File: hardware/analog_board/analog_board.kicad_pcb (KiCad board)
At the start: 4 copper layers, 105 parts, among them J1 2x5 牛角座, U1 GW2A-LV18EQ144, U2 W25Q32JVSS, U3 AD9747BCPZ

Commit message: feat：重构滤波器预布局
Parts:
- added C100: 10uF, Capacitor_SMD:C_0603_1608Metric, F.Cu at (95.8, 158.8)
- added C101: 100nF, Capacitor_SMD:C_0603_1608Metric, F.Cu at (82.9, 144.1)
- added C102: 100nF, Capacitor_SMD:C_0603_1608Metric, F.Cu at (82.9, 146.6)
- added C103: 10uF, Capacitor_SMD:C_0603_1608Metric, F.Cu at (82.9, 149.1)
- added C104: 10uF, Capacitor_SMD:C_0603_1608Metric, F.Cu at (82.8, 140.9)
- added C105: 100nF, Capacitor_SMD:C_0603_1608Metric, F.Cu at (154.7, 160.2)
- added C106: 100nF, Capacitor_SMD:C_0603_1608Metric, F.Cu at (154.7, 162.7)
- added C107: 10uF, Capacitor_SMD:C_0603_1608Metric, F.Cu at (154.7, 165.2)
- added C108: 10uF, Capacitor_SMD:C_0603_1608Metric, F.Cu at (154.7, 167.7)
- added C109: 100nF, Capacitor_SMD:C_0603_1608Metric, F.Cu at (145.2, 48.3)
- added C110: 470nF, Capacitor_SMD:C_0603_1608Metric, F.Cu at (155.0, 94.0)
- added C111: 100nF, Capacitor_SMD:C_0603_1608Metric, F.Cu at (155.0, 96.5)
- added C112: 4.7uF, Capacitor_SMD:C_0603_1608Metric, F.Cu at (155.0, 99.0)
- added C113: 470nF, Capacitor_SMD:C_0603_1608Metric, F.Cu at (155.0, 101.5)
- added C114: 100nF, Capacitor_SMD:C_0603_1608Metric, F.Cu at (159.0, 91.5)
- added C115: 4.7uF, Capacitor_SMD:C_0603_1608Metric, F.Cu at (159.0, 94.0)
- added C116: 470nF, Capacitor_SMD:C_0603_1608Metric, F.Cu at (159.0, 96.5)
- added C117: 100nF, Capacitor_SMD:C_0603_1608Metric, F.Cu at (159.0, 99.0)
- added C118: 4.7uF, Capacitor_SMD:C_0603_1608Metric, F.Cu at (159.0, 101.5)
- added C119: 470nF, Capacitor_SMD:C_0603_1608Metric, F.Cu at (163.0, 91.5)
- added C120: 100nF, Capacitor_SMD:C_0603_1608Metric, F.Cu at (163.0, 94.0)
- added C121: 100nF, Capacitor_SMD:C_0603_1608Metric, F.Cu at (214.5, 104.8)
- added C122: 100nF, Capacitor_SMD:C_0603_1608Metric, F.Cu at (214.5, 107.3)
- added C123: 330pF, Capacitor_SMD:C_0603_1608Metric, F.Cu at (214.5, 109.8)
- added C124: 33nF, Capacitor_SMD:C_0603_1608Metric, F.Cu at (214.5, 112.4)
- added C125: 1uF, Capacitor_SMD:C_0603_1608Metric, F.Cu at (214.5, 114.9)
- added C126: 1uF, Capacitor_SMD:C_0603_1608Metric, F.Cu at (214.5, 117.4)
- added C128: 100uF, Capacitor_SMD:C_Elec_6.3x7.7, F.Cu at (217.4, 66.9)
- added C129: 1uF, Capacitor_SMD:C_0603_1608Metric, F.Cu at (214.5, 119.9)
- added C130: 1uF, Capacitor_SMD:C_0603_1608Metric, F.Cu at (214.5, 122.4)
- added C131: 100nF, Capacitor_SMD:C_0603_1608Metric, F.Cu at (214.5, 124.9)
- added C133: 1uF, Capacitor_SMD:C_0603_1608Metric, F.Cu at (214.5, 127.4)
- added C134: 1uF, Capacitor_SMD:C_0603_1608Metric, F.Cu at (218.5, 104.8)
- added C135: 100nF, Capacitor_SMD:C_0603_1608Metric, F.Cu at (218.5, 107.3)
- added C136: 100nF, Capacitor_SMD:C_0603_1608Metric, F.Cu at (218.5, 109.8)
- added C137: 1.2nF, Capacitor_SMD:C_0603_1608Metric, F.Cu at (218.5, 112.4)
- added C138: 2.2uF, Capacitor_SMD:C_0603_1608Metric, F.Cu at (218.5, 114.9)
- added C139: 100uF, Capacitor_SMD:C_Elec_6.3x7.7, F.Cu at (217.4, 75.0)
- added C140: 22uF, Capacitor_SMD:C_1206_3216Metric, F.Cu at (235.3, 105.2)
- added C141: 22uF, Capacitor_SMD:C_1206_3216Metric, F.Cu at (235.3, 108.6)
- added C142: 100nF, Capacitor_SMD:C_0603_1608Metric, F.Cu at (218.5, 117.4)
- added C143: 1uF, Capacitor_SMD:C_0603_1608Metric, F.Cu at (218.5, 119.9)
- added C145: 1uF, Capacitor_SMD:C_0603_1608Metric, F.Cu at (228.3, 36.6)
- added C146: 1uF, Capacitor_SMD:C_0603_1608Metric, F.Cu at (228.3, 39.1)
- added C147: 100nF, Capacitor_SMD:C_0603_1608Metric, F.Cu at (228.3, 41.6)
- added C148: 33nF, Capacitor_SMD:C_0603_1608Metric, F.Cu at (232.3, 19.0)
- added C149: 100nF, Capacitor_SMD:C_0603_1608Metric, F.Cu at (232.3, 21.5)
- added C150: 100uF, Capacitor_SMD:C_Elec_6.3x7.7, F.Cu at (217.4, 83.2)
- added C151: 100uF, Capacitor_SMD:C_Elec_6.3x7.7, F.Cu at (217.4, 91.3)
- added C152: 22uF, Capacitor_SMD:CP_Elec_5x5.4, F.Cu at (246.8, 35.3)
- added C153: 100nF, Capacitor_SMD:C_0603_1608Metric, F.Cu at (240.6, 25.9)
- added C154: 22uF, Capacitor_SMD:C_1206_3216Metric, F.Cu at (245.2, 26.1)
- added C155: 22uF, Capacitor_SMD:C_1206_3216Metric, F.Cu at (245.2, 29.5)
- added C156: 100uF, Capacitor_SMD:C_Elec_6.3x7.7, F.Cu at (217.4, 99.5)
- added C157: 100uF, Capacitor_SMD:C_Elec_6.3x7.7, F.Cu at (227.4, 66.9)
- added C158: 100nF, Capacitor_SMD:C_0603_1608Metric, F.Cu at (222.5, 112.4)
- added C159: 100nF, Capacitor_SMD:C_0603_1608Metric, F.Cu at (222.5, 114.9)
- added C160: 100uF, Capacitor_SMD:C_Elec_6.3x7.7, F.Cu at (227.4, 75.0)
- added C161: 100uF, Capacitor_SMD:C_Elec_6.3x7.7, F.Cu at (227.4, 83.2)
- added C162: 100nF, Capacitor_SMD:C_0603_1608Metric, F.Cu at (222.5, 117.4)
- added C163: 100nF, Capacitor_SMD:C_0603_1608Metric, F.Cu at (222.5, 119.9)
- added C164: 100uF, Capacitor_SMD:C_Elec_6.3x7.7, F.Cu at (227.4, 91.3)
- added C165: 100uF, Capacitor_SMD:C_Elec_6.3x7.7, F.Cu at (227.4, 99.5)
- added C166: 1uF, Capacitor_SMD:C_0603_1608Metric, F.Cu at (222.5, 122.4)
- added C167: 100uF, Capacitor_SMD:C_Elec_6.3x7.7, F.Cu at (237.3, 66.9)
- added C168: 100uF, Capacitor_SMD:C_Elec_6.3x7.7, F.Cu at (237.3, 75.0)
- added C169: 100nF, Capacitor_SMD:C_0603_1608Metric, F.Cu at (222.5, 124.9)
- added C170: 100uF, Capacitor_SMD:C_Elec_6.3x7.7, F.Cu at (237.3, 83.2)
- added C171: 100nF, Capacitor_SMD:C_0603_1608Metric, F.Cu at (222.5, 127.4)
- added C172: 100uF, Capacitor_SMD:C_Elec_6.3x7.7, F.Cu at (237.3, 91.3)
- added C173: 100nF, Capacitor_SMD:C_0603_1608Metric, F.Cu at (226.5, 104.8)
- added C174: 100nF, Capacitor_SMD:C_0603_1608Metric, F.Cu at (226.5, 107.3)
- added C175: 10uF, Capacitor_SMD:C_0603_1608Metric, F.Cu at (226.5, 109.8)
- added C176: 10uF, Capacitor_SMD:C_0603_1608Metric, F.Cu at (226.5, 112.4)
- added C177: 100nF, Capacitor_SMD:C_0603_1608Metric, F.Cu at (226.5, 114.9)
- added C178: 22uF, Capacitor_SMD:CP_Elec_5x5.4, F.Cu at (263.7, 104.9)
- added C179: 22uF, Capacitor_SMD:CP_Elec_5x5.4, F.Cu at (195.7, 91.9)
- added C61: 56pF, Capacitor_SMD:C_0603_1608Metric, F.Cu at (119.5, 100.4)
- added C62: 100pF, Capacitor_SMD:C_0603_1608Metric, F.Cu at (119.5, 102.5)
- added C63: 100pF, Capacitor_SMD:C_0603_1608Metric, F.Cu at (119.5, 106.1)
- added C64: 62pF, Capacitor_SMD:C_0603_1608Metric, F.Cu at (119.5, 109.7)
- added C65: 56pF, Capacitor_SMD:C_0603_1608Metric, F.Cu at (116.5, 100.4)
- added C66: 100pF, Capacitor_SMD:C_0603_1608Metric, F.Cu at (116.5, 102.5)
- added C67: 100pF, Capacitor_SMD:C_0603_1608Metric, F.Cu at (116.5, 106.1)
- added C68: 62pF, Capacitor_SMD:C_0603_1608Metric, F.Cu at (116.5, 109.7)
- added C69: 6.8p, Capacitor_SMD:C_0603_1608Metric, F.Cu at (123.5, 101.5)
- added C70: 9.1p, Capacitor_SMD:C_0603_1608Metric, F.Cu at (123.8, 104.9)
- added C71: 2.0p, Capacitor_SMD:C_0603_1608Metric, F.Cu at (123.7, 108.5)
- added C72: 6.8p, Capacitor_SMD:C_0603_1608Metric, F.Cu at (112.5, 101.4)
- added C73: 9.1p, Capacitor_SMD:C_0603_1608Metric, F.Cu at (112.3, 105.1)
- added C74: 2.0p, Capacitor_SMD:C_0603_1608Metric, F.Cu at (112.5, 108.5)
- added C75: 56pF, Capacitor_SMD:C_0603_1608Metric, F.Cu at (96.6, 100.3)
- added C76: 56pF, Capacitor_SMD:C_0603_1608Metric, F.Cu at (99.6, 100.3)
- added C77: 6.8p, Capacitor_SMD:C_0603_1608Metric, F.Cu at (92.6, 101.3)
- added C78: 6.8p, Capacitor_SMD:C_0603_1608Metric, F.Cu at (103.7, 101.4)
- added C79: 100pF, Capacitor_SMD:C_0603_1608Metric, F.Cu at (96.6, 103.9)
- added C80: 100pF, Capacitor_SMD:C_0603_1608Metric, F.Cu at (99.6, 103.9)
- added C81: 9.1p, Capacitor_SMD:C_0603_1608Metric, F.Cu at (92.5, 104.9)
- added C82: 9.1p, Capacitor_SMD:C_0603_1608Metric, F.Cu at (103.7, 104.9)
- added C83: 100pF, Capacitor_SMD:C_0603_1608Metric, F.Cu at (96.6, 107.4)
- added C84: 100pF, Capacitor_SMD:C_0603_1608Metric, F.Cu at (99.6, 107.4)
- added C85: 2.0p, Capacitor_SMD:C_0603_1608Metric, F.Cu at (92.4, 108.4)
- added C86: 2.0p, Capacitor_SMD:C_0603_1608Metric, F.Cu at (103.9, 108.6)
- added C87: 62pF, Capacitor_SMD:C_0603_1608Metric, F.Cu at (96.6, 109.5)
- added C88: 62pF, Capacitor_SMD:C_0603_1608Metric, F.Cu at (99.6, 109.5)
- added C89: 100nF, Capacitor_SMD:C_0603_1608Metric, F.Cu at (145.2, 50.8)
- added C90: 100n, Capacitor_SMD:C_0603_1608Metric, F.Cu at (146.1, 144.5)
- added C91: 100nF, Capacitor_SMD:C_0603_1608Metric, F.Cu at (146.1, 147.0)
- added C92: 100nF, Capacitor_SMD:C_0603_1608Metric, F.Cu at (146.1, 149.5)
- added C93: 100nF, Capacitor_SMD:C_0603_1608Metric, F.Cu at (146.1, 152.0)
- added C94: 100nF, Capacitor_SMD:C_0603_1608Metric, F.Cu at (150.1, 142.0)
- added C95: 100n, Capacitor_SMD:C_0603_1608Metric, F.Cu at (145.5, 159.0)
- added C96: 10uF, Capacitor_SMD:C_0603_1608Metric, F.Cu at (95.8, 151.3)
- added C97: 4.7uF, Capacitor_SMD:C_0603_1608Metric, F.Cu at (155.0, 91.5)
- added C98: 100nF, Capacitor_SMD:C_0603_1608Metric, F.Cu at (95.8, 153.8)
- added C99: 100nF, Capacitor_SMD:C_0603_1608Metric, F.Cu at (95.8, 156.3)
- added D2: SS34, Diode_SMD:D_SMA, F.Cu at (179.6, 85.4)
- added D3: SS34, Diode_SMD:D_SMA, F.Cu at (179.6, 89.9)
- added FB10: 600R@100MHz, Inductor_SMD:L_0603_1608Metric, F.Cu at (158.7, 165.2)
- added FB11: 600R@100MHz, Inductor_SMD:L_0603_1608Metric, F.Cu at (163.0, 99.0)
- added FB12: 600R@100MHz, Inductor_SMD:L_0603_1608Metric, F.Cu at (163.0, 101.5)
- added FB13: 600R@100MHz, Inductor_SMD:L_0603_1608Metric, F.Cu at (167.0, 91.5)
- added FB14: 600R@100MHz, Inductor_SMD:L_0603_1608Metric, F.Cu at (167.0, 94.0)
- added FB15: 600R@100MHz, Inductor_SMD:L_0603_1608Metric, F.Cu at (167.0, 96.5)
- added FB16: 600R@100MHz, Inductor_SMD:L_0603_1608Metric, F.Cu at (167.0, 99.0)
- added FB17: 600R@100MHz, Inductor_SMD:L_0603_1608Metric, F.Cu at (167.0, 101.5)
- added FB4: 600R@100MHz, Inductor_SMD:L_0603_1608Metric, F.Cu at (163.0, 96.5)
- added FB5: 600R@100MHz, Inductor_SMD:L_0603_1608Metric, F.Cu at (100.6, 156.8)
- added FB6: 600R@100MHz, Inductor_SMD:L_0603_1608Metric, F.Cu at (100.6, 159.3)
- added FB7: 600R@100MHz, Inductor_SMD:L_0603_1608Metric, F.Cu at (86.8, 140.9)
- added FB8: 600R@100MHz, Inductor_SMD:L_0603_1608Metric, F.Cu at (86.8, 143.4)
- added FB9: 600R@100MHz, Inductor_SMD:L_0603_1608Metric, F.Cu at (158.7, 162.7)
- added HS1: Heatsink_Pad, Heatsink:TO-220_Heatsink, F.Cu at (247.7, 75.1)
- added HS2: Heatsink_Pad, Heatsink:TO-220_Heatsink, F.Cu at (247.7, 88.1)
- added HS3: Heatsink_Pad, Heatsink:TO-220_Heatsink, F.Cu at (247.7, 101.1)
- added HS4: Heatsink_Pad, Heatsink:TO-220_Heatsink, F.Cu at (247.7, 114.1)
- added J2: Conn_02x08_Counter_Clockwise, Connector_IDC:IDC-Header_2x08_P2.54mm_Latch_Vertical, F.Cu at (280.4, 74.8)
- added J3: Conn_01x04_Pin, Connector_PinHeader_2.54mm:PinHeader_1x04_P2.54mm_Vertical, F.Cu at (277.5, 108.9)
- added J4: Conn_01x08, Connector_JST:JST_VH_B8P-VH_1x08_P3.96mm_Vertical, F.Cu at (290.5, 67.5)
- added L1: 160n, Inductor_SMD:L_0805_2012Metric, F.Cu at (121.9, 101.5)
- added L10: 180n, Inductor_SMD:L_0805_2012Metric, F.Cu at (102.0, 104.9)
- added L11: 180n, Inductor_SMD:L_0805_2012Metric, F.Cu at (94.2, 108.4)
- added L12: 180n, Inductor_SMD:L_0805_2012Metric, F.Cu at (102.0, 108.5)
- added L13: 33uH, Inductor_SMD:L_Changjiang_FXL1040, F.Cu at (249.9, 120.6)
- added L14: 150uH, Inductor_SMD:L_12x12mm_H6mm, F.Cu at (265.8, 93.7)
- added L15: 2.2uH, Inductor_SMD:L_Changjiang_FXL0420, F.Cu at (271.6, 34.2)
- added L2: 180n, Inductor_SMD:L_0805_2012Metric, F.Cu at (121.9, 105.0)
- added L3: 180n, Inductor_SMD:L_0805_2012Metric, F.Cu at (121.9, 108.6)
- added L4: 160n, Inductor_SMD:L_0805_2012Metric, F.Cu at (114.1, 101.5)
- added L5: 180n, Inductor_SMD:L_0805_2012Metric, F.Cu at (114.1, 105.0)
- added L6: 180n, Inductor_SMD:L_0805_2012Metric, F.Cu at (114.1, 108.6)
- added L7: 160n, Inductor_SMD:L_0805_2012Metric, F.Cu at (94.2, 101.3)
- added L8: 160n, Inductor_SMD:L_0805_2012Metric, F.Cu at (102.0, 101.4)
- added L9: 180n, Inductor_SMD:L_0805_2012Metric, F.Cu at (94.2, 104.9)
- added Q1: MMBT3906, Package_TO_SOT_SMD:SOT-23, F.Cu at (154.2, 144.0)
- added Q2: MMBT3906, Package_TO_SOT_SMD:SOT-23, F.Cu at (154.2, 149.6)
- added R29: 53.6R, Resistor_SMD:R_0603_1608Metric, F.Cu at (96.0, 161.8)
- added R30: 226R, Resistor_SMD:R_0603_1608Metric, F.Cu at (93.5, 161.8)
- added R31: 73.2R, Resistor_SMD:R_0603_1608Metric, F.Cu at (97.0, 165.8)
- added R32: 73.2R, Resistor_SMD:R_0603_1608Metric, F.Cu at (94.5, 165.8)
- added R33: 442R, Resistor_SMD:R_0603_1608Metric, F.Cu at (92.0, 165.8)
- added R34: 442R, Resistor_SMD:R_0603_1608Metric, F.Cu at (89.5, 165.8)
- added R35: 0R, Resistor_SMD:R_0603_1608Metric, B.Cu at (117.3, 96.6)
- added R36: 10kR, Resistor_SMD:R_0603_1608Metric, F.Cu at (119.5, 111.2)
- added R37: 10kR, Resistor_SMD:R_0603_1608Metric, F.Cu at (116.5, 111.2)
- added R38: 0R, Resistor_SMD:R_0603_1608Metric, B.Cu at (98.8, 96.5)
- added R39: 10kR, Resistor_SMD:R_0603_1608Metric, F.Cu at (96.6, 111.0)
- added R40: 10kR, Resistor_SMD:R_0603_1608Metric, F.Cu at (99.6, 111.0)
- added R41: 53.6R, Resistor_SMD:R_0603_1608Metric, F.Cu at (71.8, 146.8)
- added R42: 226R, Resistor_SMD:R_0603_1608Metric, F.Cu at (77.2, 147.5)
- added R43: 73.2R, Resistor_SMD:R_0603_1608Metric, F.Cu at (74.1, 147.6)
- added R44: 73.2R, Resistor_SMD:R_0603_1608Metric, F.Cu at (75.7, 147.6)
- added R45: 442R, Resistor_SMD:R_0603_1608Metric, F.Cu at (71.8, 148.3)
- added R46: 442R, Resistor_SMD:R_0603_1608Metric, F.Cu at (78.5, 152.8)
- added R47: 100R, Resistor_SMD:R_0603_1608Metric, F.Cu at (145.2, 45.8)
- added R48: 100R, Resistor_SMD:R_0603_1608Metric, F.Cu at (145.2, 43.3)
- added R49: 68R, Resistor_SMD:R_0603_1608Metric, F.Cu at (150.1, 149.5)
- added R50: 100R, Resistor_SMD:R_0603_1608Metric, F.Cu at (150.1, 152.0)
- added R51: 68R, Resistor_SMD:R_0603_1608Metric, F.Cu at (145.5, 161.5)
- added R52: 100R, Resistor_SMD:R_0603_1608Metric, F.Cu at (145.5, 164.0)
- added R53: 10kR, Resistor_SMD:R_0402_1005Metric, F.Cu at (141.7, 51.1)
- added R54: 4.7kR, Resistor_SMD:R_0402_1005Metric, F.Cu at (141.7, 49.1)
- added R55: 4.7kR, Resistor_SMD:R_0402_1005Metric, F.Cu at (141.7, 47.1)
- added R56: 4.7kR, Resistor_SMD:R_0402_1005Metric, F.Cu at (141.6, 44.1)
- added R57: 4.7kR, Resistor_SMD:R_0402_1005Metric, F.Cu at (141.6, 46.1)
- added R58: 22R, Resistor_SMD:R_0402_1005Metric, F.Cu at (283.2, 107.6)
- added R59: 22R, Resistor_SMD:R_0402_1005Metric, F.Cu at (276.6, 121.8)
- added R60: 22R, Resistor_SMD:R_0402_1005Metric, F.Cu at (276.6, 123.8)
- added R61: 1.6kR, Resistor_SMD:R_0603_1608Metric, F.Cu at (226.5, 117.4)
- added R62: 196kR, Resistor_SMD:R_0603_1608Metric, F.Cu at (226.5, 119.9)
- added R63: 77.5k, Resistor_SMD:R_0603_1608Metric, F.Cu at (226.5, 122.4)
- added R64: 10kR, Resistor_SMD:R_0603_1608Metric, F.Cu at (226.5, 124.9)
- added R65: 237kR, Resistor_SMD:R_0603_1608Metric, F.Cu at (226.5, 127.4)
- added R66: 3.3kR, Resistor_SMD:R_0603_1608Metric, F.Cu at (230.5, 104.8)
- added R67: 77.5kR, Resistor_SMD:R_0603_1608Metric, F.Cu at (230.5, 107.3)
- added R68: 10kR, Resistor_SMD:R_0603_1608Metric, F.Cu at (230.5, 109.8)
- added R69: 15k, Resistor_SMD:R_0603_1608Metric, F.Cu at (230.5, 112.4)
- added R70: 2.4kR, Resistor_SMD:R_0603_1608Metric, F.Cu at (240.3, 29.1)
- added R71: 10kR, Resistor_SMD:R_0603_1608Metric, F.Cu at (240.3, 31.6)
- added R72: 12kR, Resistor_SMD:R_0603_1608Metric, F.Cu at (230.5, 119.9)
- added R73: 68kR, Resistor_SMD:R_0603_1608Metric, F.Cu at (230.5, 122.4)
- added R74: 7.5kR, Resistor_SMD:R_0603_1608Metric, F.Cu at (230.5, 124.9)
- added U10: TPS54360DDA, Package_SO:TI_SO-PowerPAD-8_ThermalVias, F.Cu at (187.9, 93.2)
- added U11: TPS62933, Package_TO_SOT_SMD:SOT-583-8, F.Cu at (237.5, 22.8)
- added U12: L7805, Package_TO_SOT_THT:TO-220-3_Vertical, F.Cu at (261.6, 66.7)
- added U13: L7905, Package_TO_SOT_THT:TO-220-3_Vertical, F.Cu at (261.6, 72.7)
- added U14: TPS7A4701xRGW, Package_DFN_QFN:Texas_RGW0020A_VQFN-20-1EP_5x5mm_P0.65mm_EP3.15x3.15mm_ThermalVias, F.Cu at (179.5, 100.4)
- added U15: TPS7A91, Package_DFN_QFN:Texas_S-PDSO-N10_EP1.2x2mm, F.Cu at (194.9, 85.1)
- added U16: L7815, Package_TO_SOT_THT:TO-220-3_Vertical, F.Cu at (261.6, 78.6)
- added U17: L7915, Package_TO_SOT_THT:TO-220-3_Vertical, F.Cu at (261.6, 84.6)
- added U19: AMS1117, Package_TO_SOT_SMD:SOT-223-3_TabPin2, F.Cu at (188.5, 100.6)
- added U4: OPA695ID, Package_SO:SOIC-8_3.9x4.9mm_P1.27mm, F.Cu at (89.6, 159.6)
- added U5: OPA695ID, Package_SO:SOIC-8_3.9x4.9mm_P1.27mm, F.Cu at (74.9, 152.8)
- added U6: NE5532, Package_SO:SOIC-8_3.9x4.9mm_P1.27mm, F.Cu at (133.9, 154.4)
- added U8: CDCI6214RGER, Package_DFN_QFN:VQFN-24-1EP_4x4mm_P0.5mm_EP2.45x2.45mm, F.Cu at (143.6, 38.9)
- added U9: TPS54360DDA, Package_SO:TI_SO-PowerPAD-8_ThermalVias, F.Cu at (187.9, 86.5)
- added Y1: ASE-10MHz, Oscillator:Oscillator_SMD_Abracon_ASE-4Pin_3.2x2.5mm, F.Cu at (148.8, 38.8)
- FB1: value 600R@100MHz -> 120R@100MHz
- R28: value 0R -> 4.7k
- U1: footprint ArbWave30_lib:QFP-144_20x20_Pitch0.5mm -> ArbWave30_lib:LQFP-144_20x20_Pitch0.5mm
- moved C19 73.9 mm to (117.0, 41.5), turned to -90 degrees
- moved FB3 73.1 mm to (121.7, 43.5), turned to 180 degrees
- moved R4 72.1 mm to (98.5, 41.5), turned to 90 degrees
- moved R6 71.9 mm to (100.1, 41.5), turned to 90 degrees
- moved C24 71.8 mm to (108.0, 41.5), turned to -90 degrees
- moved R5 71.7 mm to (101.6, 41.5), turned to 90 degrees
- moved C10 71.1 mm to (121.7, 45.0), turned to 180 degrees
- moved R2 69.9 mm to (130.1, 50.1), turned to 0 degrees
- moved C12 69.1 mm to (121.7, 46.6), turned to 180 degrees
- moved J1 68.6 mm to (79.3, 50.6), turned to 0 degrees
- moved R21 67.2 mm to (121.1, 47.8), turned to 90 degrees
- moved C5 66.5 mm to (121.7, 48.5), turned to 180 degrees
- moved C11 66.0 mm to (94.8, 46.5), turned to 0 degrees
- moved C4 64.4 mm to (121.7, 50.2), turned to 180 degrees
- moved U2 63.6 mm to (130.3, 55.5), turned to -90 degrees
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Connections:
- net +1.8VD renamed +1.8VD_DAC
- net +3.3VA renamed +3.3VA_DAC
- C25 pad 2: +1.8VA -> +1.8VA_DAC
- C26 pad 2: +1.8VA -> +1.8VA_DAC
- C27 pad 2: +1.8VA -> +1.8VA_DAC
- C28 pad 2: +1.8VA -> +1.8VA_DAC
- C29 pad 2: +1.8VA -> +1.8VA_DAC
- C30 pad 2: +1.8VA -> +1.8VA_DAC
- C31 pad 2: +1.8VA -> +1.8VA_DAC
- C49 pad 2: +3.3VD -> +3.3VD_DAC
- C50 pad 2: +3.3VD -> +3.3VD_DAC
- C51 pad 2: +3.3VD -> +3.3VD_DAC
- C52 pad 2: +3.3VD -> +3.3VD_DAC
- C57 pad 1: /DAC/CLKP -> /DAC/CLK+
- C57 pad 2: /DAC/CLKP -> /DAC/DAC_CLK+
- C58 pad 1: /DAC/CLKN -> /DAC/CLK-
- C58 pad 2: /DAC/CLKN -> /DAC/DAC_CLK+
- R15 pad 1: /DAC/CLKN -> /DAC/DAC_CLK+
- R15 pad 2: /DAC/CLKP -> /DAC/DAC_CLK+
- R16 pad 2: /DAC/CLKP -> /DAC/CLK+
- R17 pad 1: /DAC/CLKN -> /DAC/CLK-
- R22 pad 1: GND -> Net-(R22-Pad1)
- R23 pad 2: GND -> Net-(R22-Pad1)
- R26 pad 1: GND -> Net-(R26-Pad1)
- R26 pad 2: Net-(U3-IOUT2P) -> Net-(U3-IOUT2N)
- R27 pad 1: Net-(U3-IOUT2N) -> Net-(U3-IOUT2P)
- R27 pad 2: GND -> Net-(R26-Pad1)
- U1 pad 110: unconnected-(U1D-IOT50B-Pad110) -> /Clock/RESET_N
- U1 pad 124: unconnected-(U1C-IOT23B-Pad124) -> /FPGA/GPIO2
- U1 pad 125: unconnected-(U1C-IOT22A-Pad125) -> /FPGA/GPIO1
- U1 pad 126: unconnected-(U1C-IOT23A-Pad126) -> /FPGA/Ctrl_FPGA_NRST
- U1 pad 128: /FPGA/Ctrl_FPGA_NRST -> unconnected-(U1C-IOT19A-Pad128)
- U3 pad 1: +1.8VA -> +1.8VA_DAC
- U3 pad 27: +3.3V -> +3.3VD_DAC
- U3 pad 3: /DAC/CLKP -> /DAC/CLK+
- U3 pad 4: /DAC/CLKN -> /DAC/CLK-
- U3 pad 6: +1.8VA -> +1.8VA_DAC
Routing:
- net +1.8VA_DAC: track 0.00 -> 3.04 mm, vias 0 -> 1
- net +1.8VD_DAC: track 0.00 -> 2.21 mm, vias 0 -> 1
- net /FPGA_Config/MSPI_MCLK: track 1.85 -> 0.00 mm
- net Net-(U2-~{HOLD}/~{RESET}/IO_{3}): track 1.83 -> 0.00 mm
- net GND: vias 16 -> 9

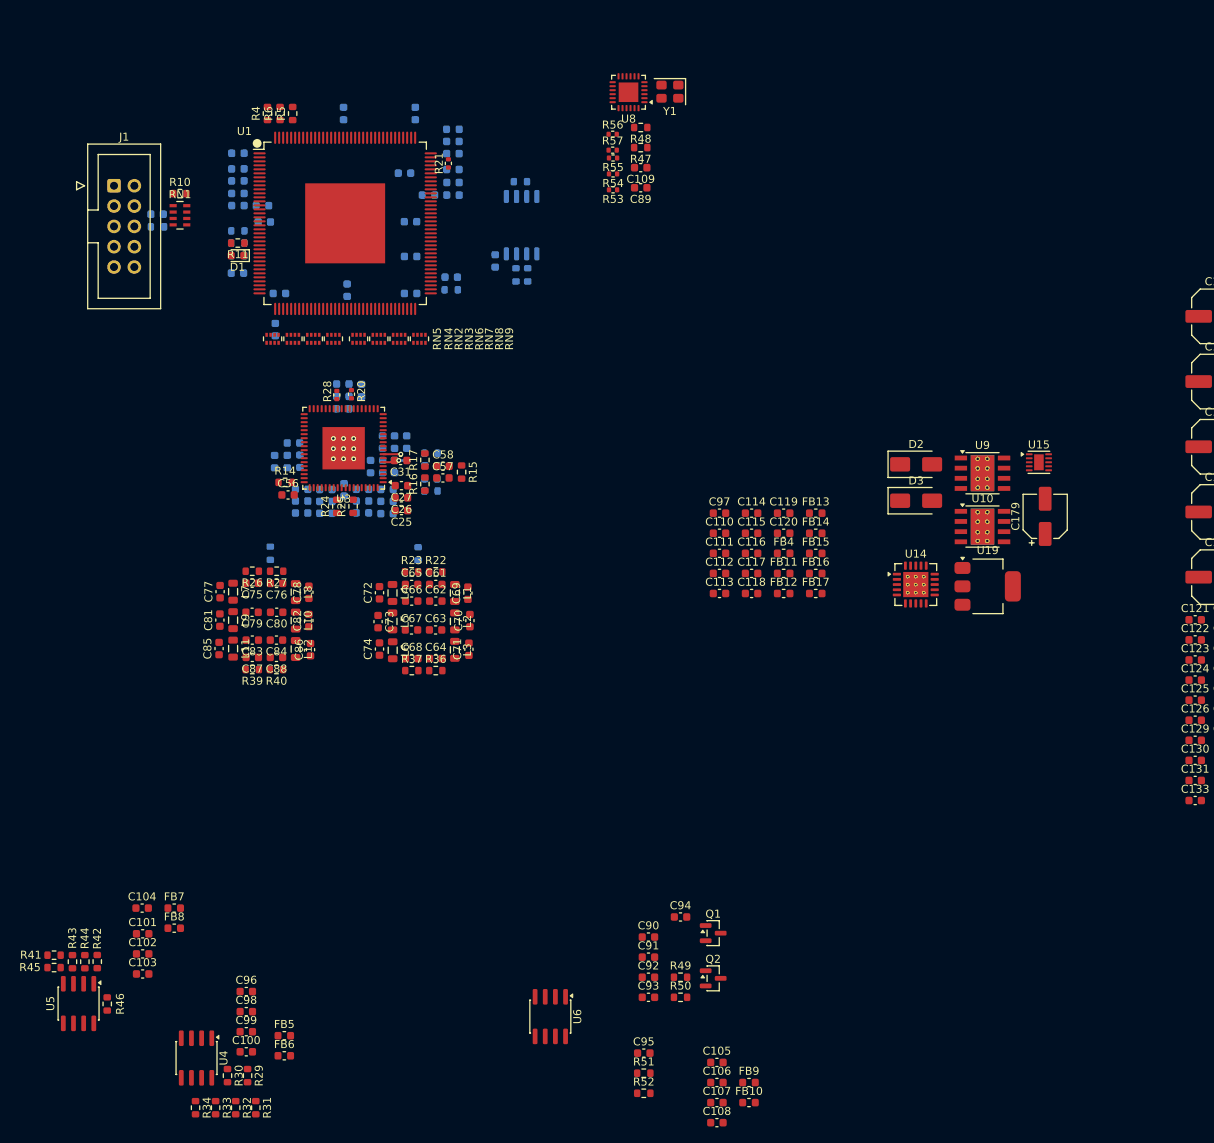
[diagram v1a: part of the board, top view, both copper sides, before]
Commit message: feat：差分转单端预布局
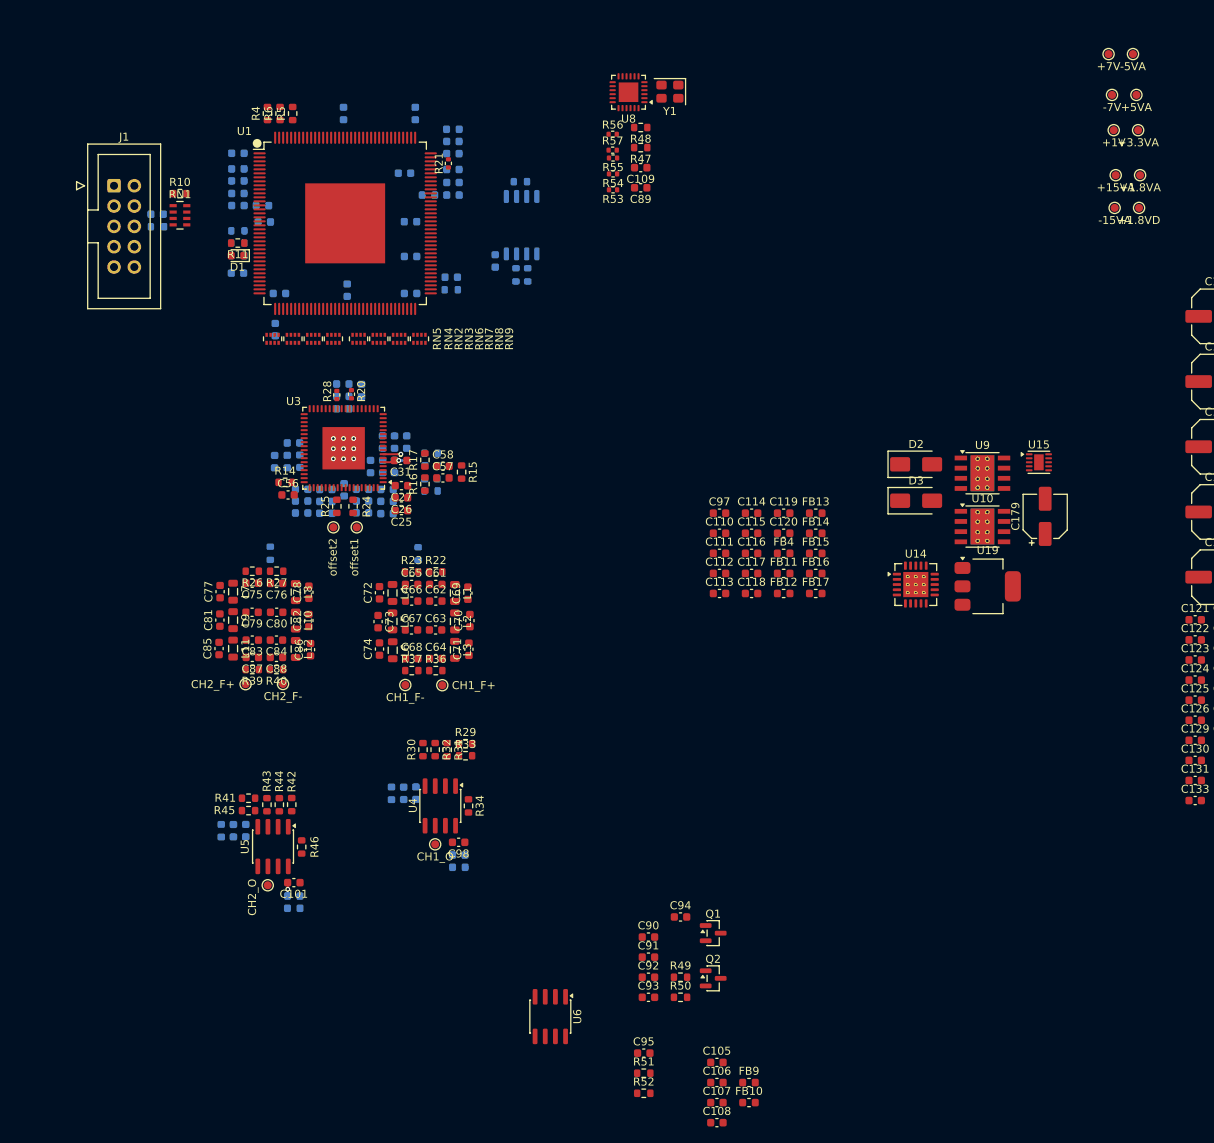
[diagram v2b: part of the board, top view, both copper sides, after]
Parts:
- added TP1: CH1_O, TestPoint:TestPoint_Pad_D1.0mm, F.Cu at (119.5, 132.9)
- added TP10: -7V, TestPoint:TestPoint_Pad_D1.0mm, F.Cu at (204.1, 39.2)
- added TP11: +1V, TestPoint:TestPoint_Pad_D1.0mm, F.Cu at (204.3, 43.6)
- added TP12: +15VA, TestPoint:TestPoint_Pad_D1.0mm, F.Cu at (204.5, 49.3)
- added TP13: -15VA, TestPoint:TestPoint_Pad_D1.0mm, F.Cu at (204.4, 53.3)
- added TP14: -5VA, TestPoint:TestPoint_Pad_D1.0mm, F.Cu at (206.7, 34.1)
- added TP15: +5VA, TestPoint:TestPoint_Pad_D1.0mm, F.Cu at (207.1, 39.2)
- added TP16: +3.3VA, TestPoint:TestPoint_Pad_D1.0mm, F.Cu at (207.3, 43.6)
- added TP17: +1.8VA, TestPoint:TestPoint_Pad_D1.0mm, F.Cu at (207.6, 49.3)
- added TP18: +1.8VD, TestPoint:TestPoint_Pad_D1.0mm, F.Cu at (207.4, 53.3)
- added TP2: CH2_O, TestPoint:TestPoint_Pad_D1.0mm, F.Cu at (98.5, 138.0)
- added TP3: CH2_F+, TestPoint:TestPoint_Pad_D1.0mm, F.Cu at (95.8, 112.9)
- added TP4: CH2_F-, TestPoint:TestPoint_Pad_D1.0mm, F.Cu at (100.4, 112.9)
- added TP5: CH1_F+, TestPoint:TestPoint_Pad_D1.0mm, F.Cu at (120.3, 113.0)
- added TP6: CH1_F-, TestPoint:TestPoint_Pad_D1.0mm, F.Cu at (115.7, 113.0)
- added TP7: offset1, TestPoint:TestPoint_Pad_D1.0mm, F.Cu at (109.7, 93.3)
- added TP8: offset2, TestPoint:TestPoint_Pad_D1.0mm, F.Cu at (106.7, 93.3)
- added TP9: +7V, TestPoint:TestPoint_Pad_D1.0mm, F.Cu at (203.6, 34.1)
- C100, C102, C103, C104, C96, C99, FB5, FB6, FB7, FB8: moved to B.Cu
- R24, R25: value 49.9R -> 499R
- moved R33 54.0 mm to (123.3, 121.8), turned to 0 degrees
- moved R32 51.2 mm to (119.5, 121.1)
- moved R34 50.9 mm to (123.6, 128.1)
- moved R31 50.7 mm to (121.0, 121.1)
- moved R29 49.6 mm to (123.3, 120.3), turned to 0 degrees
- moved R30 47.5 mm to (117.9, 121.1), turned to 90 degrees
- moved U4 43.8 mm to (120.1, 128.1)
- moved C100 37.8 mm to (115.5, 126.5), turned to -90 degrees
- moved C99 36.6 mm to (117.0, 126.5), turned to -90 degrees
- moved FB6 35.4 mm to (114.0, 126.5), turned to -90 degrees
- moved C98 33.9 mm to (122.4, 132.6), turned to 180 degrees
- moved C96 31.6 mm to (122.4, 134.2), turned to 180 degrees
- moved R41 31.2 mm to (96.1, 127.1)
- moved R42 31.2 mm to (101.5, 127.9)
- moved R43 31.2 mm to (98.4, 127.9)
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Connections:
- R25 pad 2: /DAC/offset1 -> /DAC/offset2
- U3 pad 62: /DAC/offset1 -> /DAC/offset2
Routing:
- net Net-(U5-V+): track 0.00 -> 1.53 mm, vias 0 -> 1

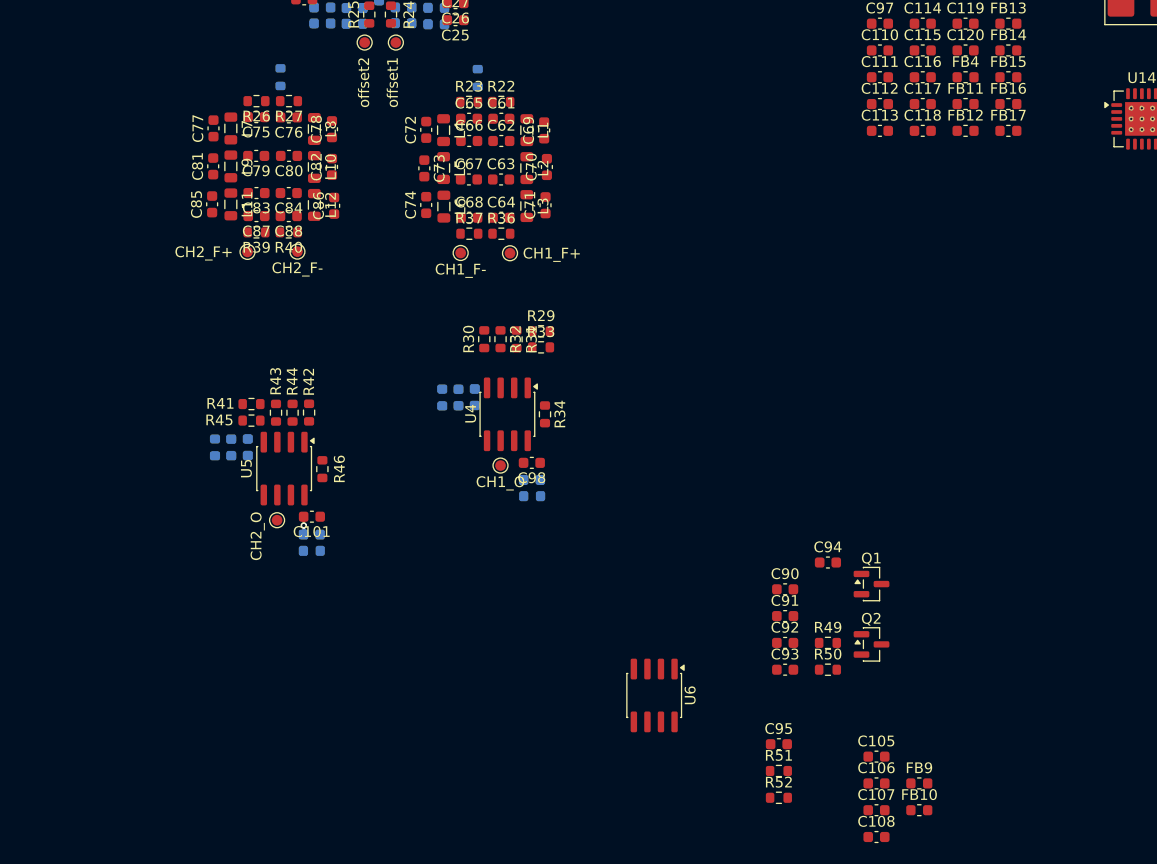
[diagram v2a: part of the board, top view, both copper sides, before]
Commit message: feat：共模反馈电路预布局
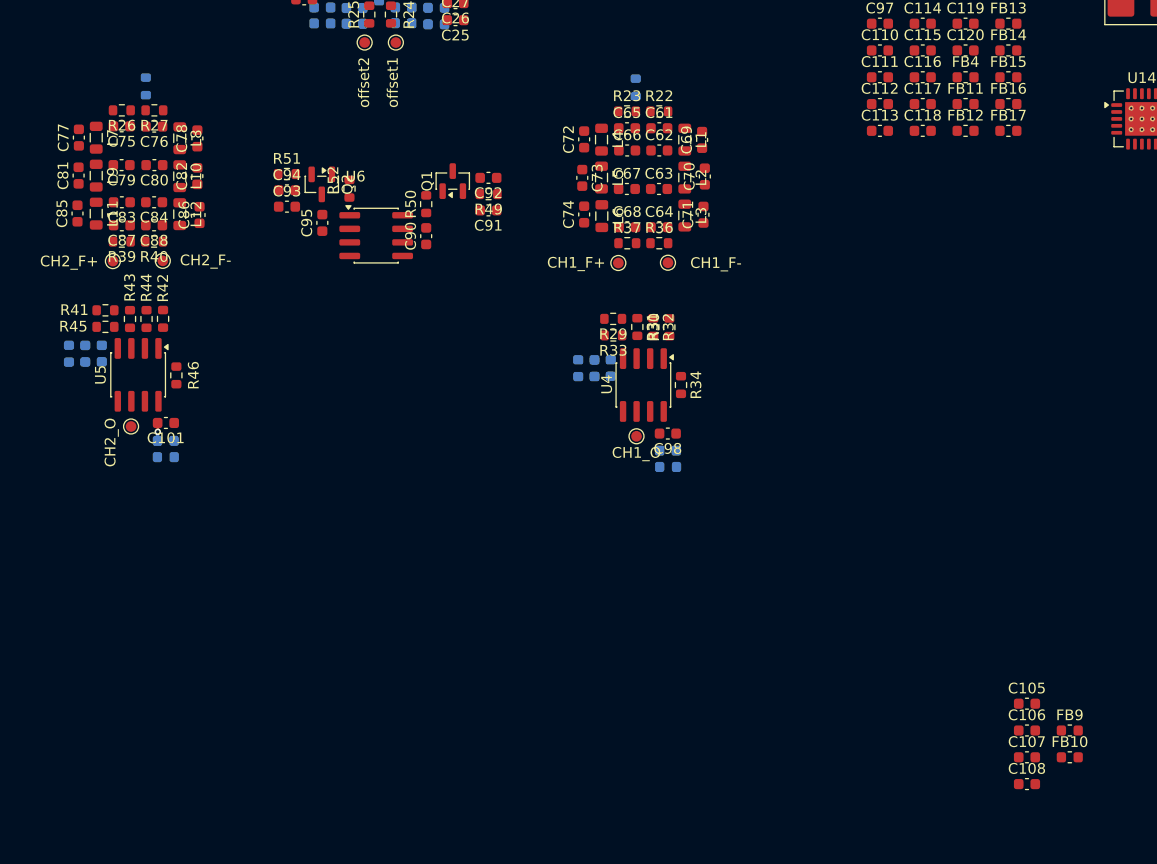
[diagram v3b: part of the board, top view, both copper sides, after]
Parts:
- moved R51 72.5 mm to (99.5, 105.6)
- moved R52 69.8 mm to (105.3, 107.0), turned to 90 degrees
- moved Q2 67.1 mm to (102.7, 106.6), turned to -90 degrees
- moved C95 64.9 mm to (102.8, 110.2), turned to 90 degrees
- moved C93 63.7 mm to (99.5, 108.6)
- moved C94 61.5 mm to (99.5, 107.1)
- moved R50 57.6 mm to (112.5, 108.4), turned to 90 degrees
- moved Q1 54.4 mm to (115.0, 106.2), turned to 90 degrees
- moved R49 52.7 mm to (118.3, 107.5), turned to 180 degrees
- moved C92 51.7 mm to (118.3, 105.9), turned to 180 degrees
- moved U6 50.3 mm to (107.8, 111.4), turned to 0 degrees
- moved C90 47.2 mm to (112.5, 111.4), turned to 90 degrees
- moved C91 47.1 mm to (118.3, 109.0), turned to 180 degrees
- moved TP6 19.4 mm to (135.1, 113.9)
- moved R30 17.4 mm to (135.3, 119.9)
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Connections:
- R29 pad 1: Net-(C64-Pad2) -> Net-(C68-Pad1)
- R30 pad 2: Net-(C68-Pad1) -> Net-(C64-Pad2)
- R31 pad 1: Net-(C64-Pad2) -> Net-(C68-Pad1)
- R32 pad 1: Net-(C68-Pad1) -> Net-(C64-Pad2)
- TP5 pad 1: Net-(C64-Pad2) -> Net-(C68-Pad1)
- TP6 pad 1: Net-(C68-Pad1) -> Net-(C64-Pad2)
